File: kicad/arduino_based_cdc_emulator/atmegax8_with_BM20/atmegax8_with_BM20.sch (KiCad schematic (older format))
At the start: 66 parts, among them IC1 ATMEGA88-A, J1 TEST_FLASH_MODE, P1 CONN_10, P2 SPI, U1 78L05-RESCUE-atmegax8_with_BM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, U2 BM20, U3 LM358, Y1 Crystal_GND24

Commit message: update
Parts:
- removed C12: 100n, Capacitors_SMD:C_0805_HandSoldering, symbol atmegax8_with_BM20-rescue:C-RESCUE-atmegax8_with_BM20
- removed JP2: FLASH_MODE, Pin_Headers.pretty:Pin_Header_Straight_1x02, symbol Device:Jumper_NO_Small
- added C6, C7: 100n, Capacitors_SMD.pretty:C_0805_HandSoldering, symbol atmegax8_with_BM20-rescue:C-RESCUE-atmegax8_with_BM20
- C1, C18, C2, C4: footprint Capacitors_SMD:C_0805_HandSoldering -> Capacitors_SMD.pretty:C_0805_HandSoldering
- C10: value 100m/25V -> CTS 47u/25V D 10% VIS-293D; footprint Capacitors_SMD:c_elec_6.3x7.7 -> Capacitors_Tantalum_SMD.pretty:TantalC_SizeD_EIA-7343_HandSoldering
- C13, C24, C25: footprint Capacitors_Tantalum_SMD:TantalC_SizeA_EIA-3216_HandSoldering -> Capacitors_Tantalum_SMD.pretty:TantalC_SizeA_EIA-3216_HandSoldering
- C14, C21, C5: footprint Capacitors_SMD:c_elec_5x5.8 -> Capacitors_SMD.pretty:c_elec_5x5.8
- C22, C28: footprint Capacitors_SMD:C_1206_HandSoldering -> Capacitors_Tantalum_SMD.pretty:TantalC_SizeA_EIA-3216_HandSoldering
- C23, C27: footprint Capacitors_SMD:C_0805_HandSoldering -> Capacitors_SMD.pretty:C_1206_HandSoldering
- C9: footprint Capacitors_SMD:c_elec_6.3x5.7 -> Capacitors_SMD.pretty:c_elec_5x5.8
- IC1: footprint Housings_QFP:TQFP-32_7x7mm_Pitch0.8mm -> Housings_QFP.pretty:LQFP-32_7x7mm_Pitch0.8mm
- JP1: footprint (none) -> Jumper:SolderJumper-3_P1.3mm_Open_RoundedPad1.0x1.5mm_NumberLabels
- P1: footprint Pin_Headers:Pin_Header_Straight_1x12 -> Pin_Headers:Pin_Header_Straight_1x12_Pitch2.54mm
- U1: footprint my_modules:SOT-223-REGULATOR -> modules:SOT-223-REGULATOR
- U2: footprint (none) -> bluetooth:BM20
- Y1: symbol Device:Crystal_GND24 -> Device:Crystal_GND3
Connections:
- net +5V: now also C6.1, C7.1
- net BTOUTL: no longer C5.2, R32.2
- net BTOUTR: now also C5.2, R32.2
- net GND: now also Y1.3, C6.2, C7.2; no longer Y1.2, Y1.4
- net at IC1.32 ((PCINT18/INT0)PD2), JP1.3 (B): no longer JP1.2 (C), R4.1
- net at IC1.7 ((PCINT6/XTAL1/TOSC1)PB6), R6.1: now also Y1.2; no longer Y1.1
- net at R5.1, R6.2: now also Y1.1; no longer Y1.3
- net +BATT: no longer names the net of U2.21 (BAT_IN)
- new net: JP1.2 (C), R4.1
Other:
- moved on the sheet: R4

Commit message: update
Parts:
- P1: symbol gencon:CONN_12 -> atmegax8_with_BM20-rescue:CONN_12-gencon
- U2: symbol BM2x:BM20 -> atmegax8_with_BM20-rescue:BM20-BM2x
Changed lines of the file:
@@
 EESchema Schematic File Version 4
 LIBS:atmegax8_with_BM20-cache
-EELAYER 26 0
+EELAYER 29 0
 EELAYER END
 $Descr A3 16535 11693
@@
 DataOut
 $Comp
-L gencon:CONN_12 P1
+L atmegax8_with_BM20-rescue:CONN_12-gencon P1
 U 1 1 530C9435
 P 8300 9900
@@
 NoConn ~ 1050 7800
 $Comp
-L BM2x:BM20 U2
+L atmegax8_with_BM20-rescue:BM20-BM2x U2
 U 1 1 5ABDEEED
 P 12650 5750

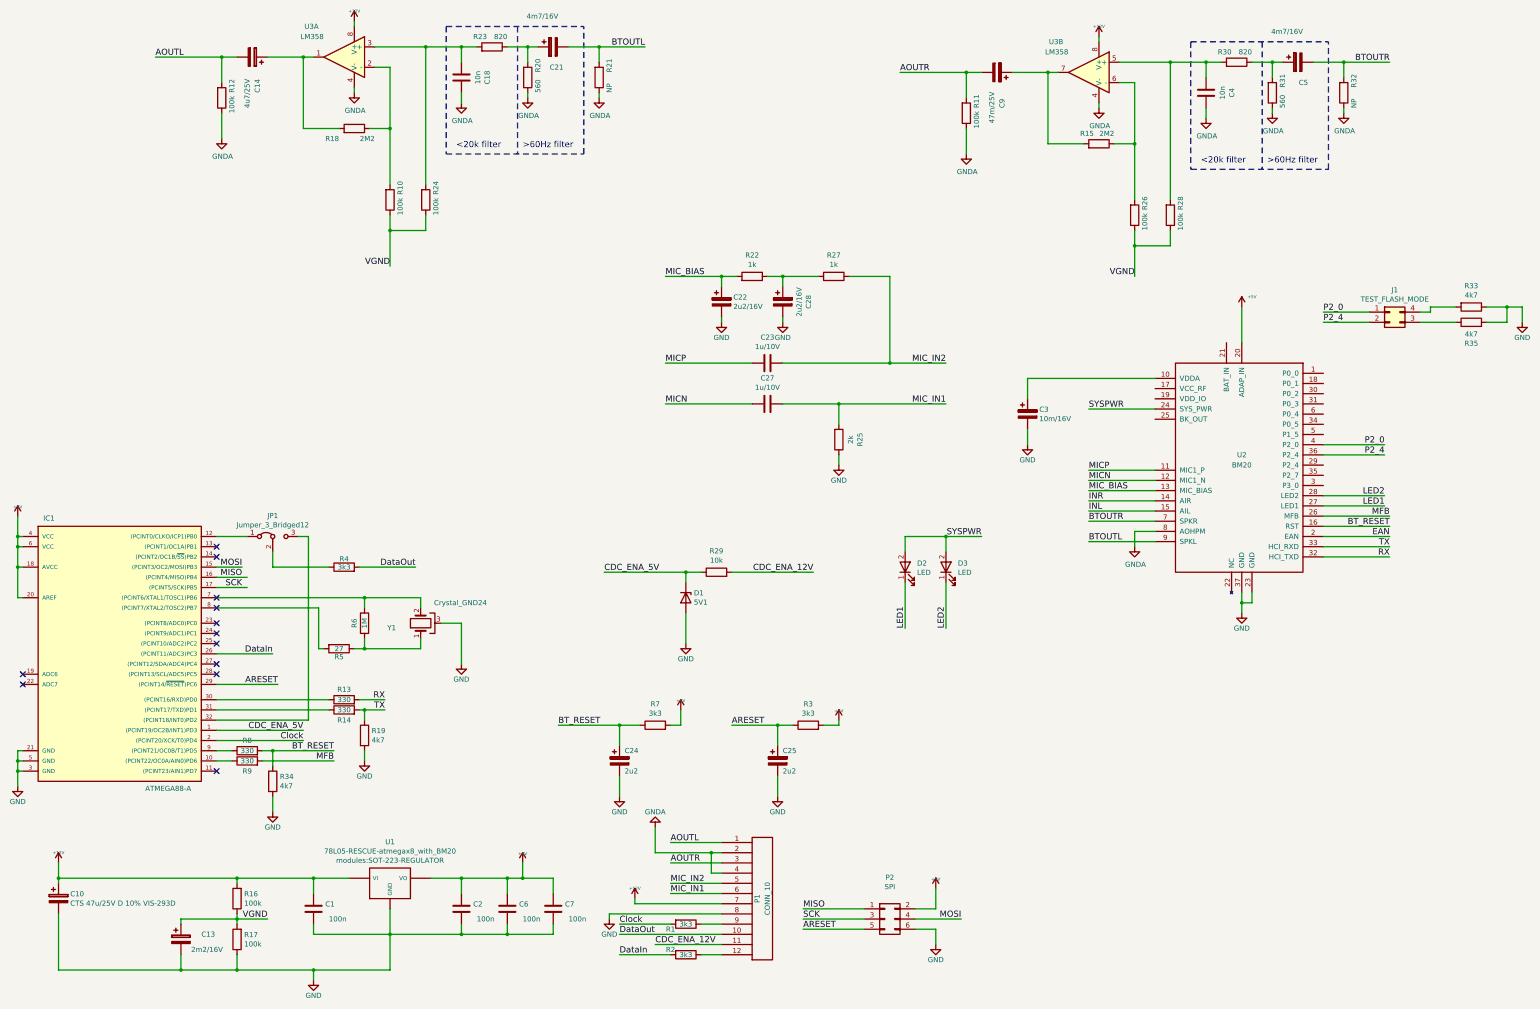
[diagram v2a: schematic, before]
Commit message: changes to BM20 version, not finished yet
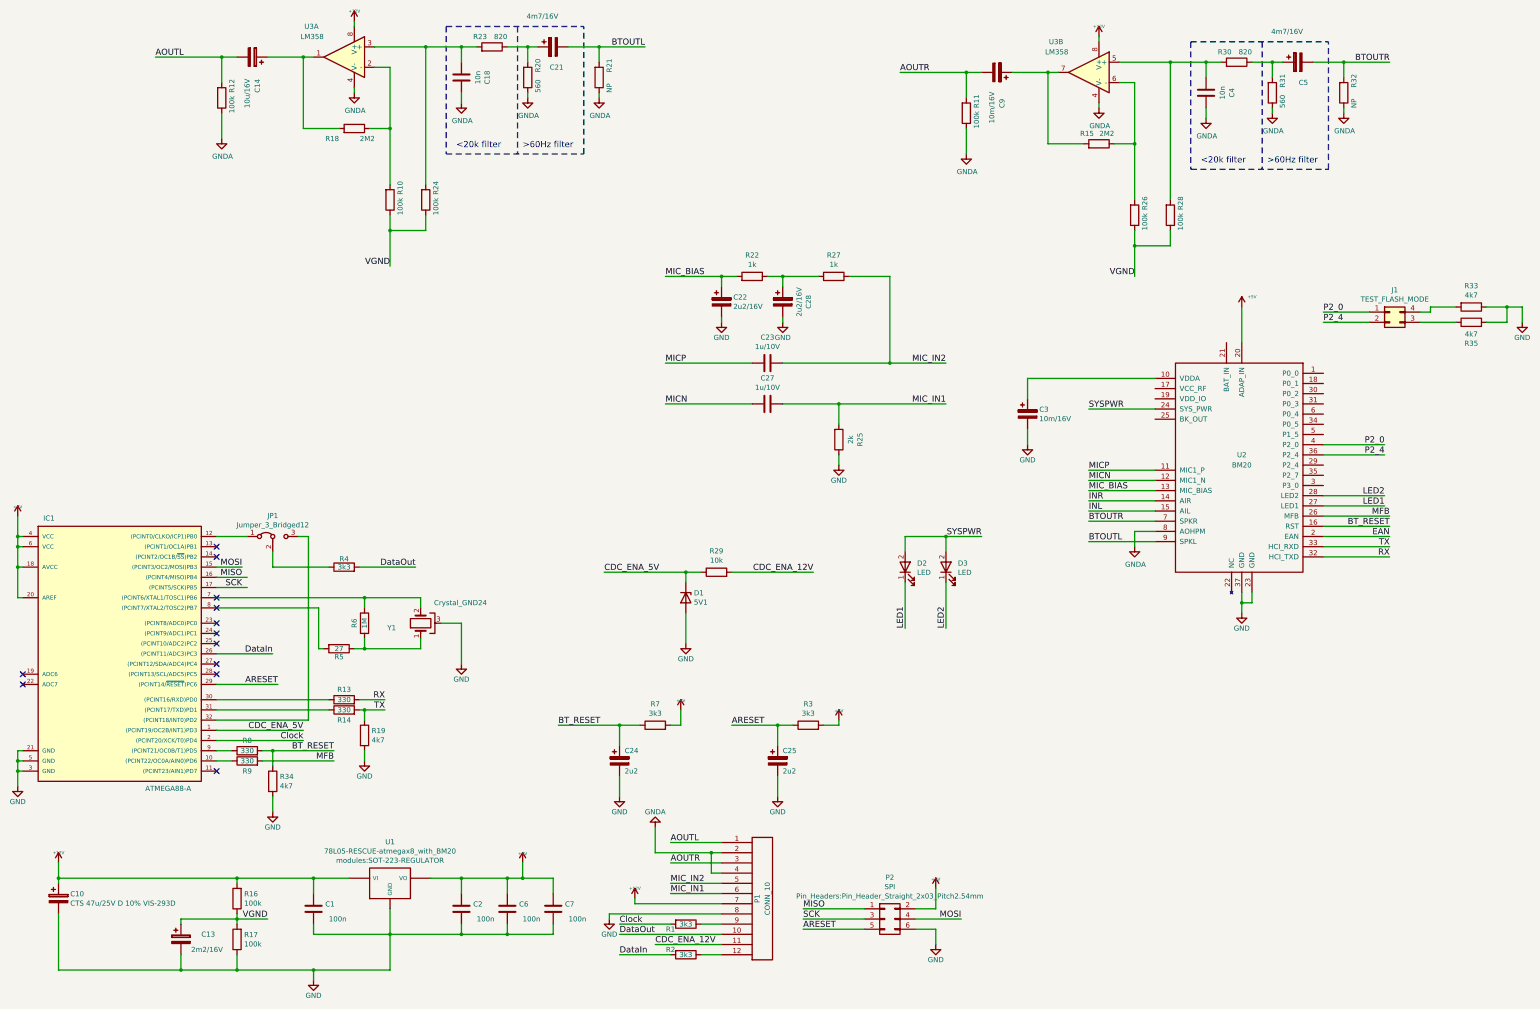
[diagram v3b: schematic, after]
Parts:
- C14: value 4u7/25V -> 10u/16V
- C9: value 47m/25V -> 10m/16V
- P2: footprint Pin_Headers:Pin_Header_Straight_2x03 -> Pin_Headers:Pin_Header_Straight_2x03_Pitch2.54mm
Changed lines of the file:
@@
-EESchema Schematic File Version 4
-LIBS:atmegax8_with_BM20-cache
-EELAYER 29 0
+EESchema Schematic File Version 5
+EELAYER 30 0
 EELAYER END
 $Descr A3 16535 11693
@@
 Comment3 ""
 Comment4 ""
+Comment5 ""
+Comment6 ""
+Comment7 ""
+Comment8 ""
+Comment9 ""
 $EndDescr
 $Comp
@@
 F 0 "P2" H 9550 10508 50  0000 C CNN
 F 1 "SPI" H 9550 10416 50  0000 C CNN
-F 2 "Pin_Headers:Pin_Header_Straight_2x03" H 9550 10324 50  0001 C CNN
+F 2 "Pin_Headers:Pin_Header_Straight_2x03_Pitch2.54mm" H 9550 10324 50  0000 C CNN
 F 3 "" H 9550 8900 50  0000 C CNN
 	1    9550 10100
@@
 P 3300 1650
 F 0 "C14" H 2950 1700 50  0000 L CNN
-F 1 "4u7/25V" H 2800 1600 50  0000 L CNN
+F 1 "10u/16V" H 2800 1600 50  0000 L CNN
 F 2 "Capacitors_SMD.pretty:c_elec_5x5.8" H 3300 1650 60  0001 C CNN
 F 3 "" H 3300 1650 60  0001 C CNN
@@
 P 10600 1800
 F 0 "C9" H 10250 1850 50  0000 L CNN
-F 1 "47m/25V" H 10100 1750 50  0000 L CNN
+F 1 "10m/16V" H 10100 1750 50  0000 L CNN
 F 2 "Capacitors_SMD.pretty:c_elec_5x5.8" H 10600 1800 60  0001 C CNN
 F 3 "" H 10600 1800 60  0001 C CNN
